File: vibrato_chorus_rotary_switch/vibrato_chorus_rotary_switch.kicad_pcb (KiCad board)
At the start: 2 copper layers, 26.4 x 20 mm, 2 parts, among them J1 7-215079-8, SW1 SW_Rotary1x6

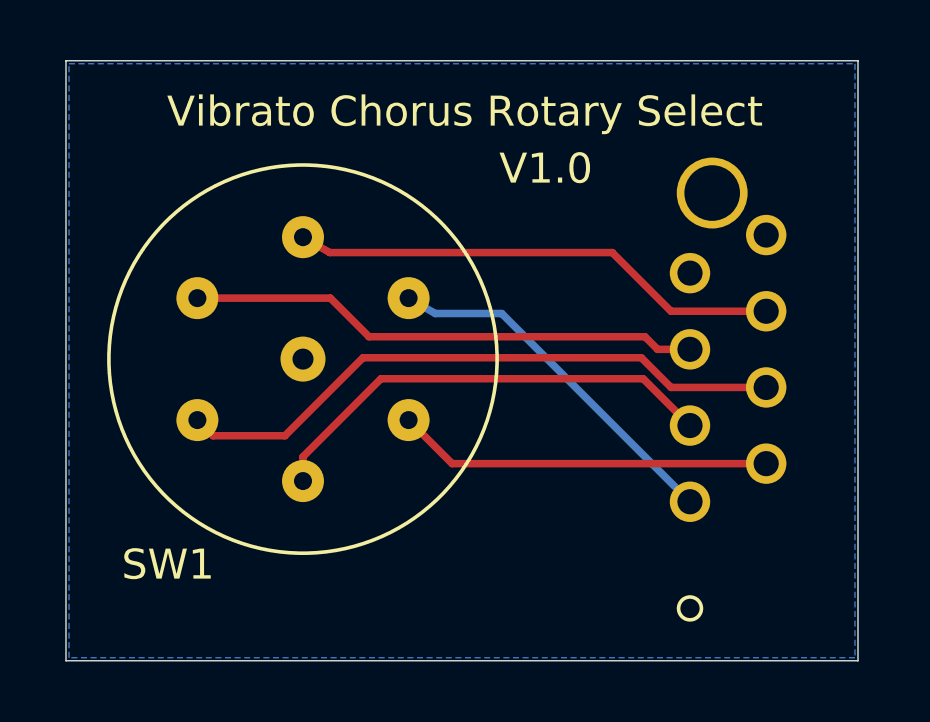
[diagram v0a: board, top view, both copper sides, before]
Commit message: A very small PCB to handle the V/C rotary switch selector
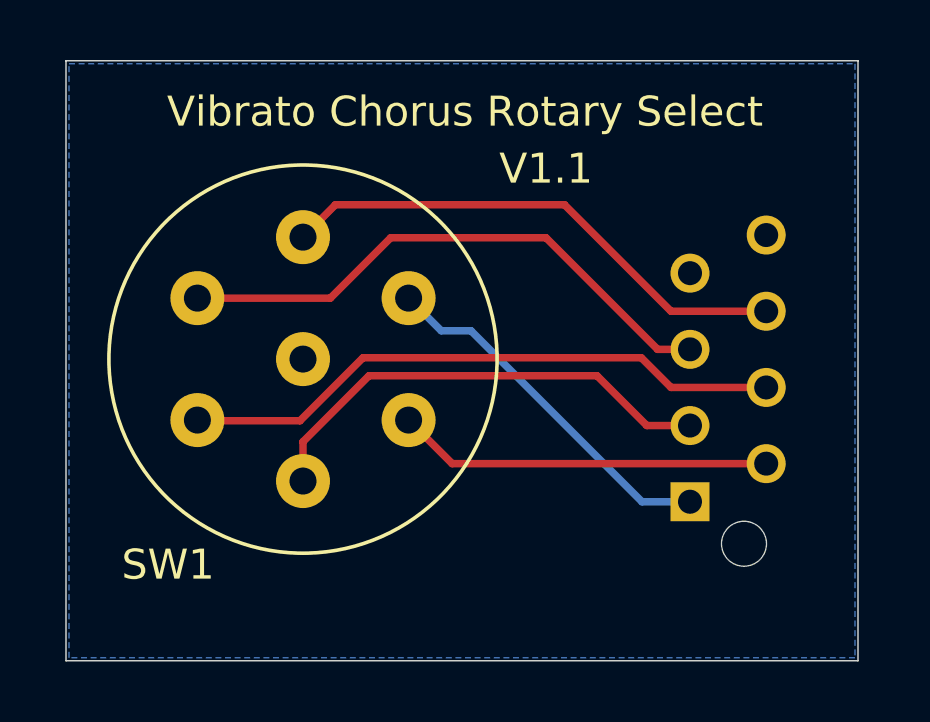
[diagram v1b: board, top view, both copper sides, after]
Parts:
- J1: footprint b3_footprints:MicroMatch_2x04_P1.27mm_Vertical -> Connector_TE-Connectivity:TE_Micro-MaTch_215079-8_2x04_P1.27mm_Vertical
- turned J1 to 0 degrees
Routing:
- net /V3: track 17.1 -> 18.8 mm
- net /C3: track 16.4 -> 17.4 mm
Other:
- board text added: "V1.1"
- board text removed: "V1.0"
